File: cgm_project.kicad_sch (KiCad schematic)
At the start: 32 parts, among them J1 JST BATT CONNECTOR, J2 USB_C_Receptacle_USB2.0_16P, J3 Conn_01x02, Q1 AO3400, SW1 SW_SPDT, SW2 BOOT, SW3 RESET, U1 TP4056-42-ESOP8, U2 AP2112K-3.3, U3 ESP32-C3-WROOM-02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

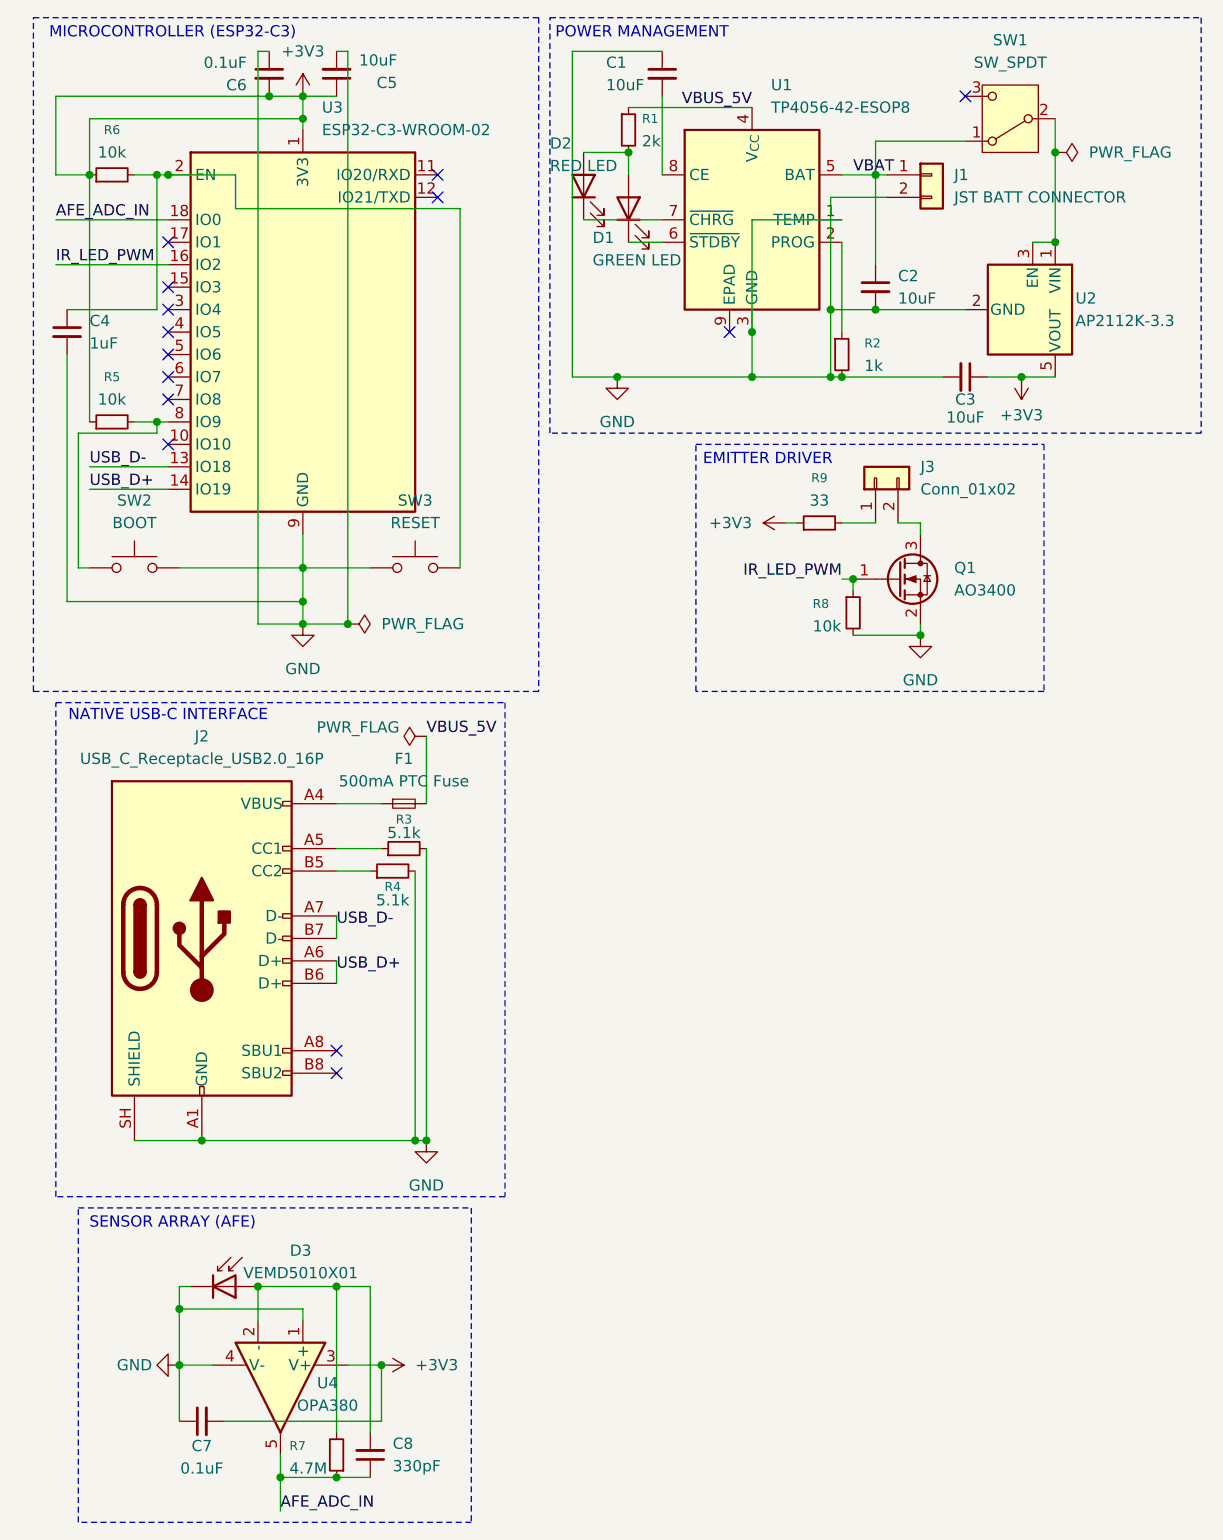
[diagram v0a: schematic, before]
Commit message: fix: resolve footprint pin mismatches for OPA380 and JST - Replace generic AFE opamp symbolw ith standard 8-pin alias, matching MSOP-8 package - Update wire harness connector to include mechanical pads for structural ground anchoring
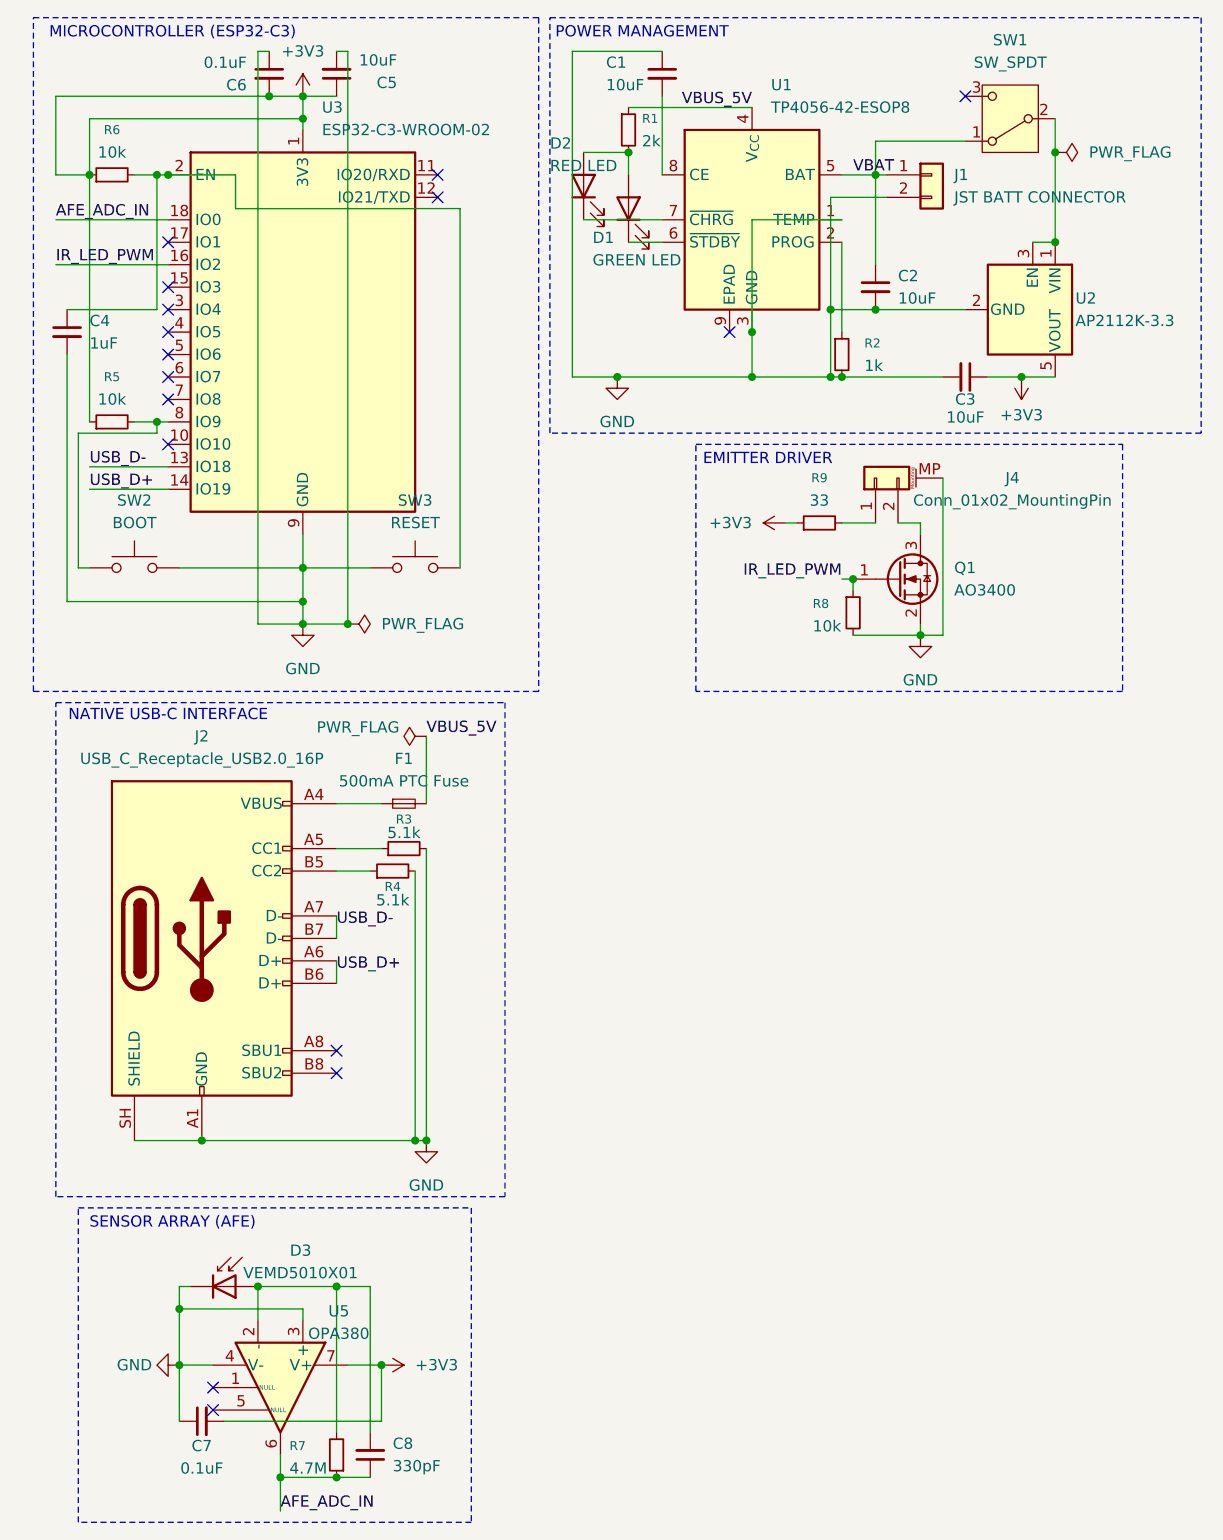
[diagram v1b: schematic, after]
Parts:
- removed J3: Conn_01x02, symbol Connector_Generic:Conn_01x02
- removed U4: OPA380, Package_SO:SOIC-8-1EP_3.9x4.9mm_P1.27mm_EP2.29x3mm, symbol Simulation_SPICE:OPAMP
- added J4: Conn_01x02_MountingPin, Connector_JST:JST_SH_SM02B-SRSS-TB_1x02-1MP_P1.00mm_Horizontal, symbol Connector_Generic_MountingPin:Conn_01x02_MountingPin
- added U5: OPA380, Package_SO:MSOP-8_3x3mm_P0.65mm, symbol Amplifier_Operational:TL071
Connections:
- net +3V3: now also U5.7 (V+)
- net AFE_ADC_IN: now also U5.6
- net GND: now also J4.MP (MountPin), U5.3 (+), U5.4 (V-)
- net at C8.2, D3.2 (A), R7.2: now also U5.2 (-)
- net at Q1.3 (D): now also J4.2 (Pin_2)
- net at R9.2: now also J4.1 (Pin_1)
- no-connect marks 14 -> 16
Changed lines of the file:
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@@
 	(rectangle
 		(start 90.17 63.5)
-		(end 129.54 91.44)
+		(end 138.43 91.44)
 		(stroke
 			(width 0)
@@
 	)
 	(no_connect
+		(at 35.56 170.18)
+	)
+	(no_connect
+		(at 35.56 172.72)
+	)
+	(no_connect
 		(at 120.65 24.13)
 	)
@@
 	(wire
 		(pts
+			(xy 118.11 85.09) (xy 115.57 85.09)
+		)
+		(stroke
+			(width 0)
+			(type default)
+		)
+	)
+	(wire
+		(pts
 			(xy 53.34 175.26) (xy 53.34 158.75)
 		)
@@
 	(wire
 		(pts
+			(xy 118.11 67.31) (xy 118.11 85.09)
+		)
+		(stroke
+			(width 0)
+			(type default)
+		)
+	)
+	(wire
+		(pts
 			(xy 107.95 85.09) (xy 115.57 85.09)
 		)
@@
 	)
 	(symbol
+		(lib_id "Amplifier_Operational:TL071")
+		(at 43.18 170.18 270)
+		(unit 1)
+		(body_style 1)
+		(exclude_from_sim no)
+		(in_bom yes)
+		(on_board yes)
+		(in_pos_files yes)
+		(dnp no)
+		(property "Reference" "U5"
+			(at 49.784 161.544 90)
+			(show_name no)
+			(do_not_autoplace no)
+			(effects
+				(font
+					(size 1.27 1.27)
+				)
+			)
+		)
+		(property "Value" "OPA380"
+			(at 49.784 164.084 90)
+			(show_name no)
+			(do_not_autoplace no)
+			(effects
+				(font
+					(size 1.27 1.27)
+				)
+			)
+		)
+		(property "Footprint" "Package_SO:MSOP-8_3x3mm_P0.65mm"
+			(at 44.45 171.45 0)
+			(hide yes)
+			(show_name no)
+			(do_not_autoplace no)
+			(effects
+				(font
+					(size 1.27 1.27)
+				)
+			)
+		)
+		(property "Datasheet" "http://www.ti.com/lit/ds/symlink/tl071.pdf"
+			(at 46.99 173.99 0)
+			(hide yes)
+			(show_name no)
+			(do_not_autoplace no)
+			(effects
+				(font
+					(size 1.27 1.27)
+				)
+			)
+		)
+		(property "Description" "Single Low-Noise JFET-Input Operational Amplifiers, DIP-8/SOIC-8"
+			(at 43.18 170.18 0)
+			(hide yes)
+			(show_name no)
+			(do_not_autoplace no)
+			(effects
+				(font
+					(size 1.27 1.27)
+				)
+			)
+		)
+		(pin "1"
+		)
+		(pin "5"
+		)
+		(pin "6"
+		)
+		(pin "8"
+		)
+		(pin "4"
+		)
+		(pin "7"
+		)
+		(pin "2"
+		)
+		(pin "3"
+		)
+		(instances
+			(project "cgm_project"
+				(path "/56312daa-544d-4a20-aa90-3dd296ddb5b0"
+					(reference "U5")
+					(unit 1)
+				)
+			)
+		)
+	)
+	(symbol
 		(lib_id "Device:LED")
 		(at 82.55 36.83 90)
@@
 	)
 	(symbol
-		(lib_id "Simulation_SPICE:OPAMP")
-		(at 43.18 170.18 270)
+		(lib_id "Device:R_Small")
+		(at 49.53 177.8 180)
 		(unit 1)
 		(body_style 1)
@@
 		(in_pos_files yes)
 		(dnp no)
-		(property "Reference" "U4"
-			(at 48.514 169.672 90)
-			(show_name no)
-			(do_not_autoplace no)
-			(effects
-				(font
-					(size 1.27 1.27)
-				)
-			)
-		)
-		(property "Value" "OPA380"
-			(at 48.514 172.212 90)
-			(show_name no)
-			(do_not_autoplace no)
-			(effects
-				(font
-					(size 1.27 1.27)
-				)
-			)
-		)
-		(property "Footprint" "Package_SO:SOIC-8-1EP_3.9x4.9mm_P1.27mm_EP2.29x3mm"
-			(at 43.18 170.18 0)
-			(hide yes)
-			(show_name no)
-			(do_not_autoplace no)
-			(effects
-				(font
-					(size 1.27 1.27)
-				)
-			)
-		)
-		(property "Datasheet" "https://ngspice.sourceforge.io/docs/ngspice-html-manual/manual.xhtml#sec__SUBCKT_Subcircuits"
-			(at 43.18 170.18 0)
-			(hide yes)
-			(show_name no)
-			(do_not_autoplace no)
-			(effects
-				(font
-					(size 1.27 1.27)
-				)
-			)
-		)
-		(property "Description" "Operational amplifier, single"
-			(at 43.18 170.18 0)
-			(hide yes)
+		(property "Reference" "R7"
+			(at 44.196 176.784 0)
 			(show_name no)
 			(do_not_autoplace no)
 			(effects
 				(font
-					(size 1.27 1.27)
+					(size 1.016 1.016)
 				)
+				(justify right)
 			)
 		)
-		(property "Sim.Pins" "1=in+ 2=in- 3=vcc 4=vee 5=out"
-			(at 43.18 170.18 0)
-			(hide yes)
+		(property "Value" "4.7M"
+			(at 44.196 179.324 0)
 			(show_name no)
 			(do_not_autoplace no)
@@
 					(size 1.27 1.27)
 				)
+				(justify right)
 			)
 		)
-		(property "Sim.Device" "SUBCKT"
-			(at 43.18 170.18 0)
+		(property "Footprint" "Resistor_SMD:R_0805_2012Metric"
+			(at 49.53 177.8 0)
 			(hide yes)
 			(show_name no)
@@
 					(size 1.27 1.27)
 				)
-				(justify left)
 			)
 		)
-		(property "Sim.Library" "${KICAD9_SYMBOL_DIR}/Simulation_SPICE.sp"
-			(at 43.18 170.18 0)
+		(property "Datasheet" ""
+			(at 49.53 177.8 0)
 			(hide yes)
 			(show_name no)
@@
 			)
 		)
-		(property "Sim.Name" "kicad_builtin_opamp"
-			(at 43.18 170.18 0)
+		(property "Description" "Resistor, small symbol"
+			(at 49.53 177.8 0)
 			(hide yes)
 			(show_name no)
@@
 		(pin "1"
 		)
-		(pin "5"
-		)
-		(pin "3"
-		)
 		(pin "2"
 		)
-		(pin "4"
-		)
 		(instances
 			(project "cgm_project"
 				(path "/56312daa-544d-4a20-aa90-3dd296ddb5b0"
-					(reference "U4")
+					(reference "R7")
 					(unit 1)
 				)
@@
 	)
 	(symbol
-		(lib_id "Device:R_Small")
-		(at 49.53 177.8 180)
+		(lib_id "Connector_Generic_MountingPin:Conn_01x02_MountingPin")
+		(at 110.49 67.31 90)
 		(unit 1)
 		(body_style 1)
@@
 		(in_pos_files yes)
 		(dnp no)
-		(property "Reference" "R7"
-			(at 44.196 176.784 0)
+		(property "Reference" "J4"
+			(at 125.984 67.31 90)
 			(show_name no)
 			(do_not_autoplace no)
 			(effects
 				(font
-					(size 1.016 1.016)
+					(size 1.27 1.27)
 				)
-				(justify right)
 			)
 		)
-		(property "Value" "4.7M"
-			(at 44.196 179.324 0)
+		(property "Value" "Conn_01x02_MountingPin"
+			(at 125.984 69.85 90)
 			(show_name no)
 			(do_not_autoplace no)
@@
 					(size 1.27 1.27)
 				)
-				(justify right)
 			)
 		)
-		(property "Footprint" "Resistor_SMD:R_0805_2012Metric"
-			(at 49.53 177.8 0)
+		(property "Footprint" "Connector_JST:JST_SH_SM02B-SRSS-TB_1x02-1MP_P1.00mm_Horizontal"
+			(at 110.49 67.31 0)
 			(hide yes)
 			(show_name no)
@@
 		)
 		(property "Datasheet" ""
-			(at 49.53 177.8 0)
+			(at 110.49 67.31 0)
 			(hide yes)
 			(show_name no)
@@
 			)
 		)
-		(property "Description" "Resistor, small symbol"
-			(at 49.53 177.8 0)
+		(property "Description" "Generic connectable mounting pin connector, single row, 01x02, script generated (kicad-library-utils/schlib/autogen/connector/)"
+			(at 110.49 67.31 0)
 			(hide yes)
 			(show_name no)
@@
 			)
 		)
-		(pin "1"
+		(pin "MP"
 		)
 		(pin "2"
 		)
+		(pin "1"
+		)
 		(instances
 			(project "cgm_project"
 				(path "/56312daa-544d-4a20-aa90-3dd296ddb5b0"
-					(reference "R7")
+					(reference "J4")
 					(unit 1)
 				)
@@
 					(unit 1)
 				)
-			)
-		)
-	)
-	(symbol
-		(lib_id "Connector_Generic:Conn_01x02")
-		(at 110.49 67.31 90)
-		(unit 1)
-		(body_style 1)
-		(exclude_from_sim no)
-		(in_bom yes)
-		(on_board yes)
-		(in_pos_files yes)
-		(dnp no)
-		(fields_autoplaced yes)
-		(property "Reference" "J3"
-			(at 115.57 66.0399 90)
-			(show_name no)
-			(do_not_autoplace no)
-			(effects
-				(font
-					(size 1.27 1.27)
-				)
-				(justify right)
-			)
-		)
-		(property "Value" "Conn_01x02"
-			(at 115.57 68.5799 90)
-			(show_name no)
-			(do_not_autoplace no)
-			(effects
-				(font
-					(size 1.27 1.27)
-				)
-				(justify right)
-			)
-		)
-		(property "Footprint" ""
-			(at 110.49 67.31 0)
-			(hide yes)
-			(show_name no)
-			(do_not_autoplace no)
-			(effects
-				(font
-					(size 1.27 1.27)
-				)
-			)
-		)
-		(property "Datasheet" ""
-			(at 110.49 67.31 0)
-			(hide yes)
-			(show_name no)
-			(do_not_autoplace no)
-			(effects
-				(font
-					(size 1.27 1.27)
-				)
-			)
-		)
-		(property "Description" "Generic connector, single row, 01x02, script generated (kicad-library-utils/schlib/autogen/connector/)"
-			(at 110.49 67.31 0)
-			(hide yes)
-			(show_name no)
-			(do_not_autoplace no)
-			(effects
-				(font
-					(size 1.27 1.27)
-				)
-			)
-		)
-		(pin "1"
-		)
-		(pin "2"
-		)
-		(instances
-			(project "cgm_project"
-				(path "/56312daa-544d-4a20-aa90-3dd296ddb5b0"
-					(reference "J3")
-					(unit 1)
-				)

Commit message: chore: switched to a double sided design - changed BOOT and RST to a more compact footpritn - moved all connectors and switches to front of board
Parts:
- SW2, SW3: footprint Button_Switch_SMD:SW_SPST_FSMSM -> Button_Switch_SMD:SW_SPST_B3U-1000P
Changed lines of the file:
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@@
 			)
 		)
-		(property "Footprint" "Button_Switch_SMD:SW_SPST_FSMSM"
+		(property "Footprint" "Button_Switch_SMD:SW_SPST_B3U-1000P"
 			(at 26.67 72.39 0)
 			(hide yes)
@@
 			)
 		)
-		(property "Footprint" "Button_Switch_SMD:SW_SPST_FSMSM"
+		(property "Footprint" "Button_Switch_SMD:SW_SPST_B3U-1000P"
 			(at 58.42 72.39 0)
 			(hide yes)

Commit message: chore: placement of decoupling resistors and capacitors on bottom of PCB
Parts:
- renumbered J4 to J3, U5 to U4
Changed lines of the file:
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@@
 		(in_pos_files yes)
 		(dnp no)
-		(property "Reference" "U5"
+		(property "Reference" "U4"
 			(at 49.784 161.544 90)
 			(show_name no)
@@
 			(project "cgm_project"
 				(path "/56312daa-544d-4a20-aa90-3dd296ddb5b0"
-					(reference "U5")
+					(reference "U4")
 					(unit 1)
 				)
@@
 		(in_pos_files yes)
 		(dnp no)
-		(property "Reference" "J4"
+		(property "Reference" "J3"
 			(at 125.984 67.31 90)
 			(show_name no)
@@
 			(project "cgm_project"
 				(path "/56312daa-544d-4a20-aa90-3dd296ddb5b0"
-					(reference "J4")
+					(reference "J3")
 					(unit 1)
 				)

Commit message: chore: add M2 mounting hole
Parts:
- added H1: MountingHole, MountingHole:MountingHole_2.2mm_M2, symbol Mechanical:MountingHole
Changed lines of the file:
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@@
+	)
+	(symbol
+		(lib_id "Mechanical:MountingHole")
+		(at 55.88 88.9 0)
+		(unit 1)
+		(body_style 1)
+		(exclude_from_sim no)
+		(in_bom no)
+		(on_board yes)
+		(in_pos_files yes)
+		(dnp no)
+		(fields_autoplaced yes)
+		(property "Reference" "H1"
+			(at 58.42 87.6299 0)
+			(show_name no)
+			(do_not_autoplace no)
+			(effects
+				(font
+					(size 1.27 1.27)
+				)
+				(justify left)
+			)
+		)
+		(property "Value" "MountingHole"
+			(at 58.42 90.1699 0)
+			(show_name no)
+			(do_not_autoplace no)
+			(effects
+				(font
+					(size 1.27 1.27)
+				)
+				(justify left)
+			)
+		)
+		(property "Footprint" "MountingHole:MountingHole_2.2mm_M2"
+			(at 55.88 88.9 0)
+			(hide yes)
+			(show_name no)
+			(do_not_autoplace no)
+			(effects
+				(font
+					(size 1.27 1.27)
+				)
+			)
+		)
+		(property "Datasheet" ""
+			(at 55.88 88.9 0)
+			(hide yes)
+			(show_name no)
+			(do_not_autoplace no)
+			(effects
+				(font
+					(size 1.27 1.27)
+				)
+			)
+		)
+		(property "Description" "Mounting Hole without connection"
+			(at 55.88 88.9 0)
+			(hide yes)
+			(show_name no)
+			(do_not_autoplace no)
+			(effects
+				(font
+					(size 1.27 1.27)
+				)
+			)
+		)
+		(instances
+			(project "cgm_project"
+				(path "/56312daa-544d-4a20-aa90-3dd296ddb5b0"
+					(reference "H1")
+					(unit 1)
+				)
+			)
+		)
 	)
 	(symbol
